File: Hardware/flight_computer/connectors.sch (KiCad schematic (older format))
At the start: 14 parts, among them J4 JST_8_RA, J5 JST_GH_6_RA, J6 JST_GH_4_RA, J7 JST_GH_5_RA, J8 Conn_02x03, J9 Conn_02x03, U4 Dual_XOR_GATE, U5 Dual_XOR_GATE

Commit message: Finishes v1 connections
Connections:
- net 3V3 renamed VDD_3V3_STM
- net VDD_3V3_STM: no longer J7.4
- new net VDD_3V3_RADIO: J7.4
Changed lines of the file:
@@
 Text HLabel 4150 1350 2    50   Input ~ 0
 SWDIO
-Text HLabel 3650 1150 0    50   Input ~ 0
-3V3
-Text HLabel 1450 5350 2    50   Input ~ 0
-3V3
 Text Label 1400 3900 0    50   ~ 0
 tx_frsky
@@
 Wire Wire Line
 	4000 4000 4000 4100
-Text HLabel 4950 3700 2    50   Input ~ 0
-3V3
 Text HLabel 3900 3700 0    50   Input ~ 0
 FrSky_INV
@@
 Wire Wire Line
 	3950 5350 3950 5400
-Text HLabel 4900 5050 2    50   Input ~ 0
-3V3
 Text HLabel 4900 5250 2    50   Input ~ 0
 FMU_RC_OUTPUT
@@
 Text HLabel 1950 3800 2    50   Input ~ 0
 VDD_5V_RADIO
+Text HLabel 1450 5350 2    50   Input ~ 0
+VDD_3V3_RADIO
+Text HLabel 4950 3700 2    50   Input ~ 0
+VDD_3V3_STM
+Text HLabel 4900 5050 2    50   Input ~ 0
+VDD_3V3_STM
+Text HLabel 3650 1150 0    50   Input ~ 0
+VDD_3V3_STM
 $EndSCHEMATC

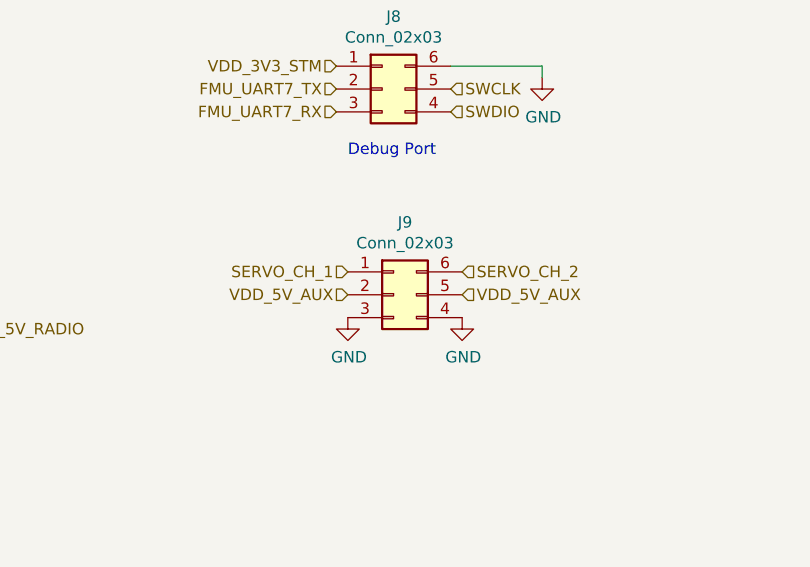
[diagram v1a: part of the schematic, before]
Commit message: Thickens gps power trace and updates servo connector pins
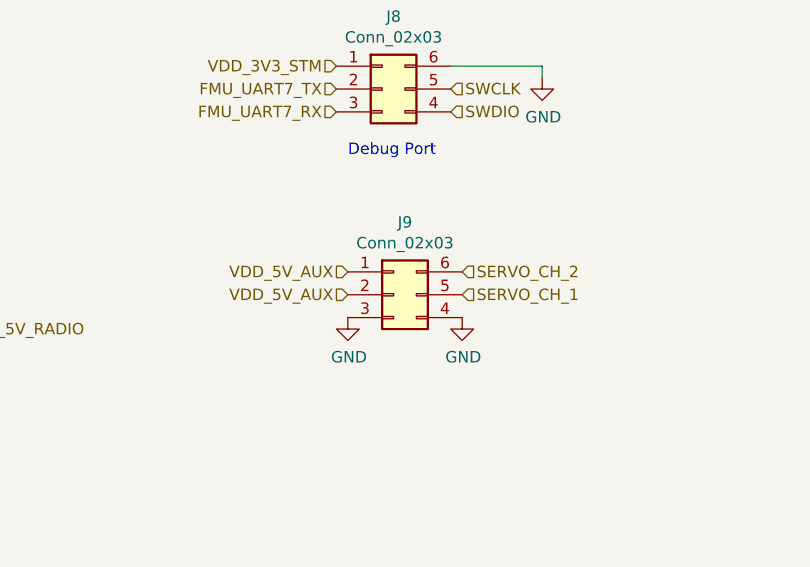
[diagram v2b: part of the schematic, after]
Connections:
- net SERVO_CH_1: now also J9.5 (Pin_5); no longer J9.1 (Pin_1)
- net VDD_5V_AUX: now also J9.1 (Pin_1); no longer J9.5 (Pin_5)
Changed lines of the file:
@@
 	1    0    0    -1
 $EndComp
+Text HLabel 3700 2050 0    50   Input ~ 0
+VDD_5V_AUX
 Text HLabel 3700 2150 0    50   Input ~ 0
 VDD_5V_AUX
 Text HLabel 4200 2150 2    50   Input ~ 0
-VDD_5V_AUX
-Text HLabel 3700 2050 0    50   Input ~ 0
 SERVO_CH_1
 Text HLabel 4200 2050 2    50   Input ~ 0

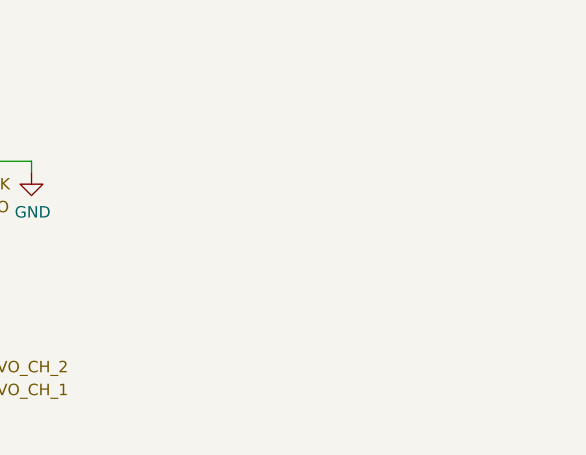
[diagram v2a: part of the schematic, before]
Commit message: Adds 2-pin battery connector
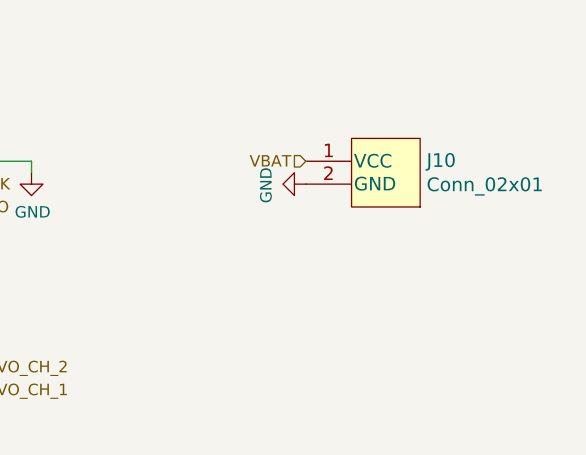
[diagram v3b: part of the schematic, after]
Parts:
- added J10: Conn_02x01, drone_footprints:TSW-102-07-F-S, symbol openDrone_parts:Conn_02x01
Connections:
- net GND: now also J10.2 (GND)
- net VBAT: now also J10.1 (VCC)
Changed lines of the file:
@@
 Text HLabel 3650 1150 0    50   Input ~ 0
 VDD_3V3_STM
+$Comp
+L openDrone_parts:Conn_02x01 J10
+U 1 1 5F91158E
+P 5750 1150
+F 0 "J10" H 6278 1153 60  0000 L CNN
+F 1 "Conn_02x01" H 6278 1047 60  0000 L CNN
+F 2 "drone_footprints:TSW-102-07-F-S" H 6050 900 60  0001 C CNN
+F 3 "https://www.digikey.com/en/products/detail/samtec-inc/TSW-102-07-F-S/2685866" H 5750 1150 60  0001 C CNN
+F 4 "SAM10844-ND" H 5800 1400 50  0001 C CNN "DPN"
+	1    5750 1150
+	1    0    0    -1
+$EndComp
+Text HLabel 5750 1150 0    50   Input ~ 0
+VBAT
+$Comp
+L power:GND #PWR0103
+U 1 1 5F911EF0
+P 5750 1250
+F 0 "#PWR0103" H 5750 1000 50  0001 C CNN
+F 1 "GND" H 5755 1077 50  0000 C CNN
+F 2 "" H 5750 1250 50  0001 C CNN
+F 3 "" H 5750 1250 50  0001 C CNN
+	1    5750 1250
+	0    1    1    0
+$EndComp
 $EndSCHEMATC
